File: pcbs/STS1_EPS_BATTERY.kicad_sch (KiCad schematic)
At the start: 11 parts, among them J3 Battery Pack, Q4 SI7272DP-T1-GE3, U13 TMCS1101A3B-Q1, U4 BQ29209DRBT

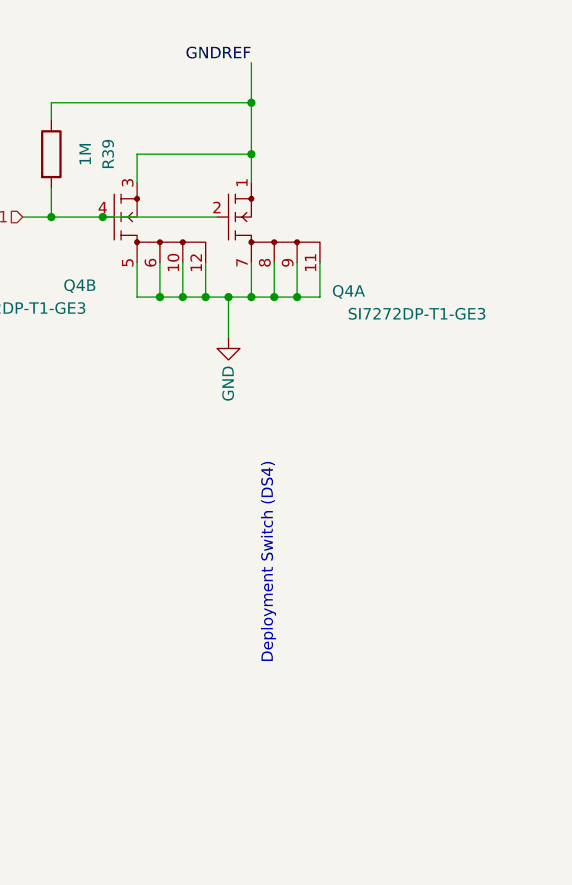
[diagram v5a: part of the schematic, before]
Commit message: Added testpoints to STS1_EPS_1.
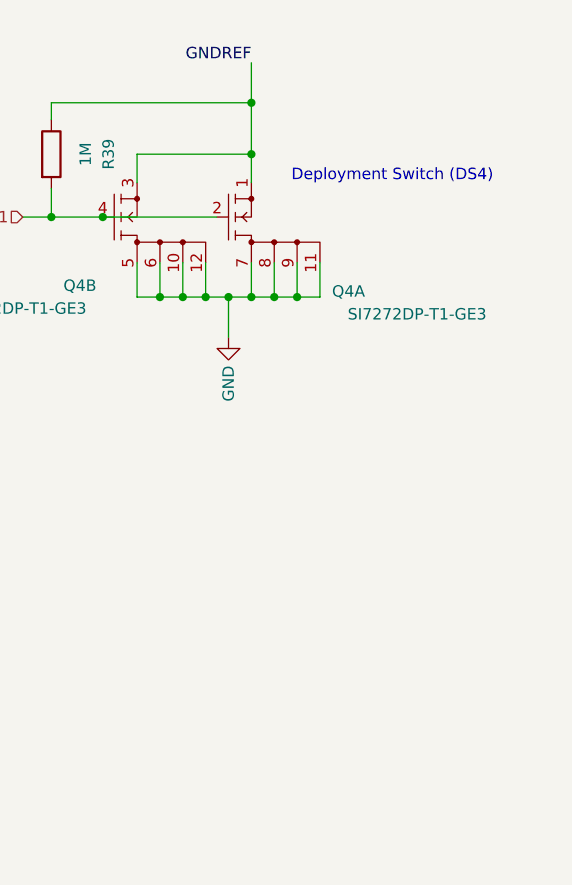
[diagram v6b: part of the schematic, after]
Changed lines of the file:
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@@
     (effects (font (size 1.27 1.27)) (justify left bottom))
   )
-  (text "Deployment Switch (DS4)" (at 234.315 76.2 270)
-    (effects (font (size 1.27 1.27)) (justify right bottom))
+  (text "Deployment Switch (DS4)" (at 236.22 45.085 0)
+    (effects (font (size 1.27 1.27)) (justify left bottom))
   )
   (text "Overvoltage detection is not used." (at 114.3 87.63 0)
